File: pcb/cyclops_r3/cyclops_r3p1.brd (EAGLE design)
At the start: 69.8 x 53.3 mm, 48 parts, among them Q1 SUM11006, Q2 IRF510, U1 MCP4921, U2 317-N, U3 ADR03, U4 OP1177, U5 LM324N, U6 ZXTD45

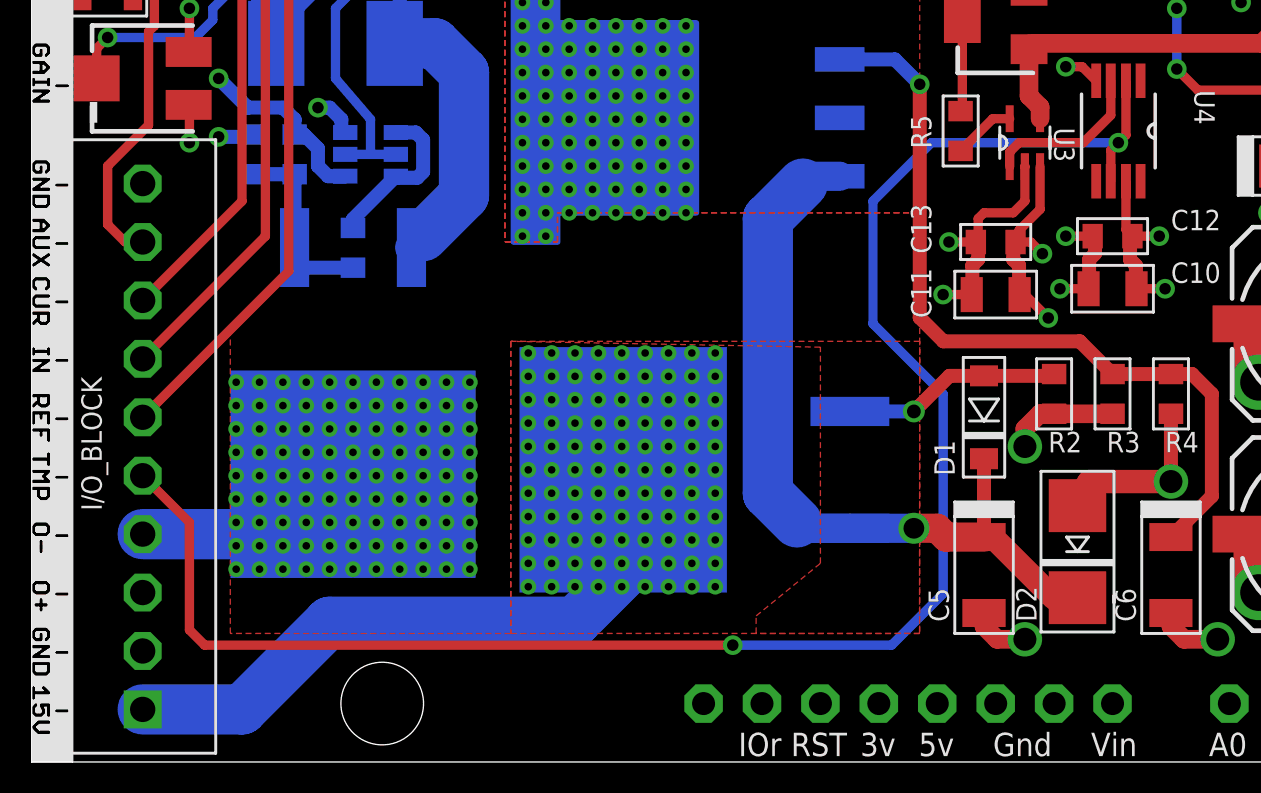
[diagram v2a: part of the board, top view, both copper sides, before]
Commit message: Small routing improvement.
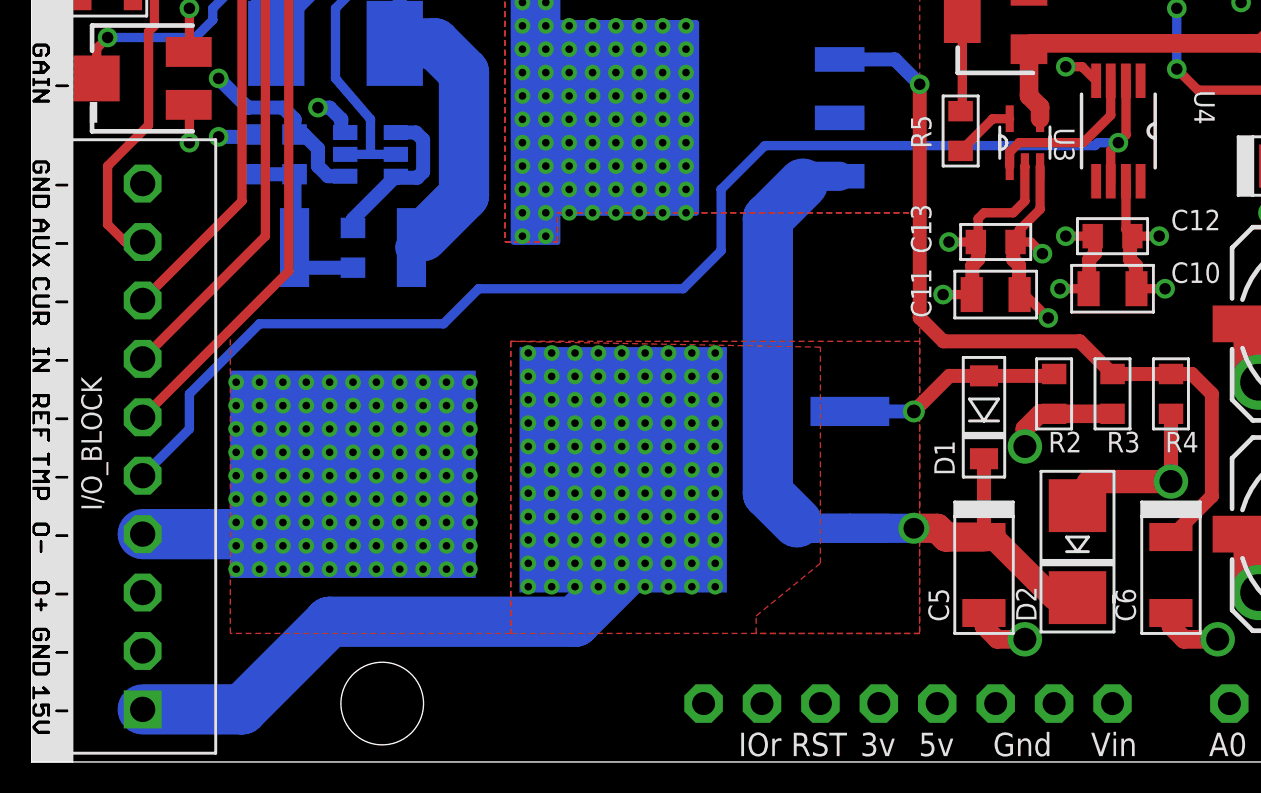
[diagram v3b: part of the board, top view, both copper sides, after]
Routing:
- net VTEMP: track 76.2 -> 55.5 mm, vias 2 -> 1
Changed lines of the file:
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@@
 <layers>
 <layer number="1" name="Top" color="4" fill="1" visible="yes" active="yes"/>
-<layer number="2" name="Route2" color="1" fill="3" visible="yes" active="yes"/>
+<layer number="2" name="Route2" color="1" fill="3" visible="no" active="yes"/>
 <layer number="3" name="Route3" color="4" fill="3" visible="no" active="no"/>
 <layer number="4" name="Route4" color="1" fill="4" visible="no" active="no"/>
@@
 <layer number="13" name="Route13" color="4" fill="5" visible="no" active="no"/>
 <layer number="14" name="Route14" color="1" fill="6" visible="no" active="no"/>
-<layer number="15" name="Route15" color="4" fill="6" visible="yes" active="yes"/>
-<layer number="16" name="Bottom" color="1" fill="1" visible="yes" active="yes"/>
-<layer number="17" name="Pads" color="2" fill="1" visible="yes" active="yes"/>
-<layer number="18" name="Vias" color="2" fill="1" visible="yes" active="yes"/>
-<layer number="19" name="Unrouted" color="6" fill="1" visible="yes" active="yes"/>
-<layer number="20" name="Dimension" color="15" fill="1" visible="yes" active="yes"/>
-<layer number="21" name="tPlace" color="7" fill="1" visible="yes" active="yes"/>
-<layer number="22" name="bPlace" color="7" fill="1" visible="yes" active="yes"/>
-<layer number="23" name="tOrigins" color="15" fill="1" visible="yes" active="yes"/>
-<layer number="24" name="bOrigins" color="15" fill="1" visible="yes" active="yes"/>
-<layer number="25" name="tNames" color="7" fill="1" visible="yes" active="yes"/>
-<layer number="26" name="bNames" color="7" fill="1" visible="yes" active="yes"/>
-<layer number="27" name="tValues" color="7" fill="1" visible="yes" active="yes"/>
-<layer number="28" name="bValues" color="7" fill="1" visible="yes" active="yes"/>
+<layer number="15" name="Route15" color="4" fill="6" visible="no" active="yes"/>
+<layer number="16" name="Bottom" color="1" fill="1" visible="no" active="yes"/>
+<layer number="17" name="Pads" color="2" fill="1" visible="no" active="yes"/>
+<layer number="18" name="Vias" color="2" fill="1" visible="no" active="yes"/>
+<layer number="19" name="Unrouted" color="6" fill="1" visible="no" active="yes"/>
+<layer number="20" name="Dimension" color="15" fill="1" visible="no" active="yes"/>
+<layer number="21" name="tPlace" color="7" fill="1" visible="no" active="yes"/>
+<layer number="22" name="bPlace" color="7" fill="1" visible="no" active="yes"/>
+<layer number="23" name="tOrigins" color="15" fill="1" visible="no" active="yes"/>
+<layer number="24" name="bOrigins" color="15" fill="1" visible="no" active="yes"/>
+<layer number="25" name="tNames" color="7" fill="1" visible="no" active="yes"/>
+<layer number="26" name="bNames" color="7" fill="1" visible="no" active="yes"/>
+<layer number="27" name="tValues" color="7" fill="1" visible="no" active="yes"/>
+<layer number="28" name="bValues" color="7" fill="1" visible="no" active="yes"/>
 <layer number="29" name="tStop" color="7" fill="3" visible="yes" active="yes"/>
 <layer number="30" name="bStop" color="7" fill="6" visible="no" active="yes"/>
@@
 <wire x1="45.6438" y1="26.5938" x2="45.6438" y2="25.2476" width="0.4064" layer="1"/>
 <via x="45.974" y="26.924" extent="1-16" drill="0.5"/>
-<wire x1="45.974" y1="26.924" x2="37.846" y2="26.924" width="0.4064" layer="16"/>
+<wire x1="45.974" y1="26.924" x2="45.085" y2="26.924" width="0.4064" layer="16"/>
+<wire x1="45.085" y1="26.924" x2="44.958" y2="26.797" width="0.4064" layer="16"/>
+<wire x1="44.958" y1="26.797" x2="30.607" y2="26.797" width="0.4064" layer="16"/>
 <contactref element="I/O_BLOCK" pad="P$5"/>
-<wire x1="37.846" y1="26.924" x2="35.306" y2="24.384" width="0.4064" layer="16"/>
-<wire x1="35.306" y1="24.384" x2="35.306" y2="19.05" width="0.4064" layer="16"/>
-<wire x1="35.306" y1="19.05" x2="38.354" y2="16.002" width="0.4064" layer="16"/>
-<wire x1="38.354" y1="16.002" x2="38.354" y2="7.317803125" width="0.4064" layer="16"/>
-<wire x1="38.354" y1="7.317803125" x2="36.116196875" y2="5.08" width="0.4064" layer="16"/>
-<wire x1="36.116196875" y1="5.08" x2="29.21" y2="5.08" width="0.4064" layer="16"/>
-<wire x1="29.21" y1="5.08" x2="6.249809375" y2="5.08" width="0.4064" layer="1"/>
-<wire x1="6.249809375" y1="5.08" x2="5.588" y2="5.741809375" width="0.4064" layer="1"/>
-<wire x1="5.588" y1="5.741809375" x2="5.588" y2="10.414" width="0.4064" layer="1"/>
-<wire x1="5.588" y1="10.414" x2="3.556" y2="12.446" width="0.4064" layer="1"/>
 <wire x1="45.6438" y1="26.5938" x2="45.974" y2="26.924" width="0.4064" layer="1"/>
 <wire x1="45.974" y1="26.924" x2="46.3042" y2="27.2542" width="0.4064" layer="1"/>
-<via x="29.21" y="5.08" extent="1-16" drill="0.5"/>
+<wire x1="30.607" y1="26.797" x2="28.702" y2="24.892" width="0.4064" layer="16"/>
+<wire x1="28.702" y1="24.892" x2="28.702" y2="22.225" width="0.4064" layer="16"/>
+<wire x1="28.702" y1="22.225" x2="27.051" y2="20.574" width="0.4064" layer="16"/>
+<wire x1="27.051" y1="20.574" x2="18.161" y2="20.574" width="0.4064" layer="16"/>
+<wire x1="18.161" y1="20.574" x2="16.637" y2="19.05" width="0.4064" layer="16"/>
+<wire x1="16.637" y1="19.05" x2="8.636" y2="19.05" width="0.4064" layer="16"/>
+<wire x1="8.636" y1="19.05" x2="5.588" y2="16.002" width="0.4064" layer="16"/>
+<wire x1="5.588" y1="16.002" x2="5.588" y2="14.478" width="0.4064" layer="16"/>
+<wire x1="5.588" y1="14.478" x2="3.556" y2="12.446" width="0.4064" layer="16"/>
 </signal>
 <signal name="VCTL">

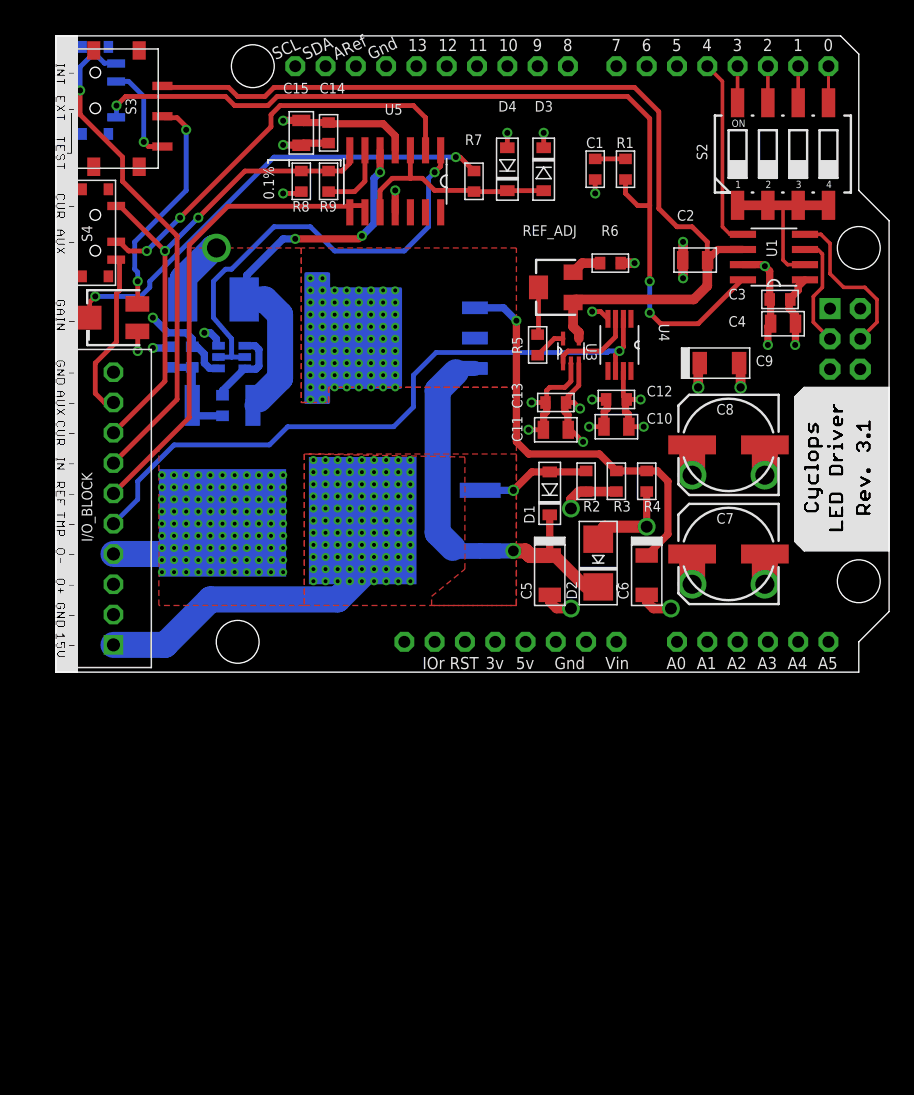
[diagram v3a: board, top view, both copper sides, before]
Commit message: Added a low profile BNC connection for getting input from an amplified photodiode.
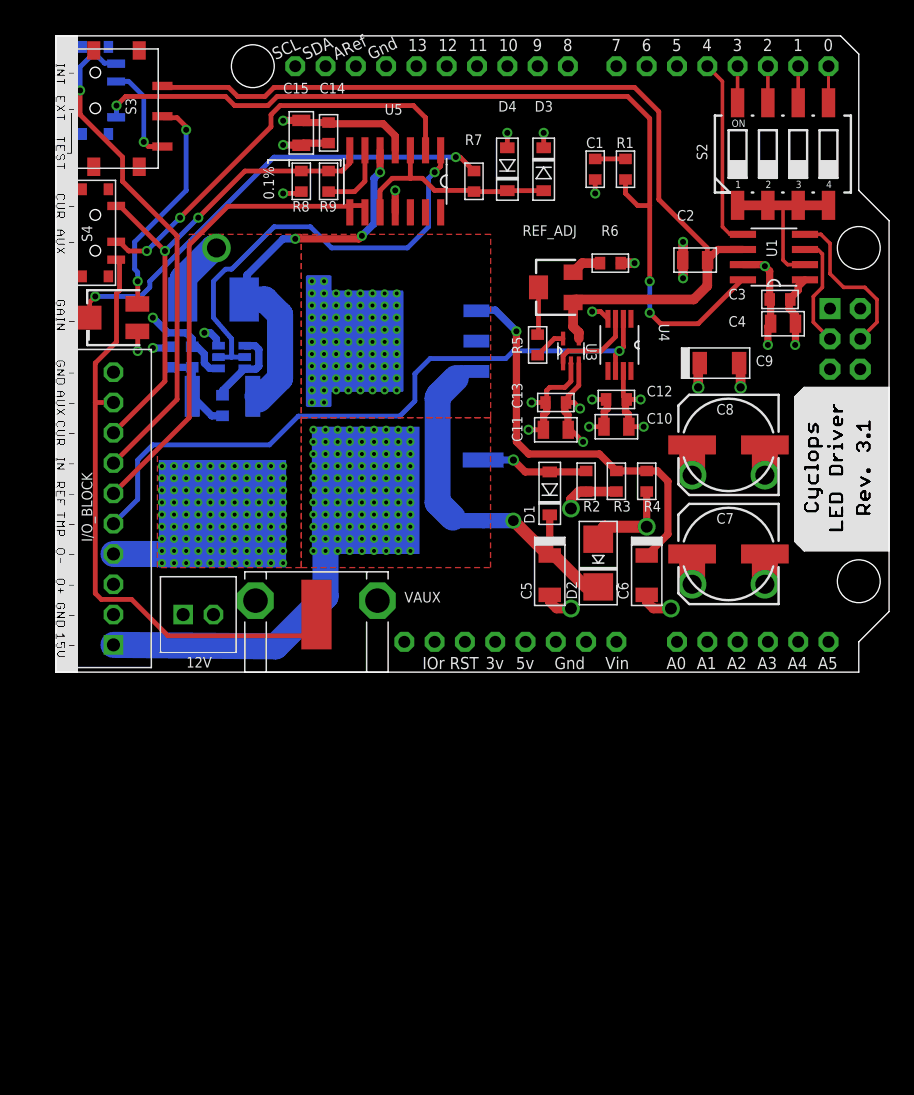
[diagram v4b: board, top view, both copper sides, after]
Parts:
- added 12V: SCREW2, cyclops:SCREW2
- added VAUX: (no value), cyclops:361V509E
- moved Q1 2.55 mm to (29.2, 15.2)
- moved Q2 0.76 mm to (12.7, 17.8)
- moved U2 0.28 mm to (26.8, 27.7)
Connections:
- net +12V: now also 12V.P$2
- net GND: now also 12V.P$1, VAUX.2, VAUX.3
- net VAUX: now also VAUX.1
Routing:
- net VAUX: track 14.0 -> 54.9 mm
- net LED-: track 10.4 -> 18.7 mm
- net +15V: track 28.8 -> 32.0 mm
- net +15V_RECT: track 34.9 -> 33.0 mm
- net N$13: track 8.60 -> 7.42 mm
- net VTEMP: track 55.5 -> 56.3 mm
- net REFA: track 79.1 -> 78.4 mm
- net N$72: track 35.1 -> 34.4 mm

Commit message: Added a note concerning the location of the MOSFET pre-biasing.
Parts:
- R3: value 1.8k -> 2.1k
- R4: value 240k -> 240
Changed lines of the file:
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@@
 <attribute name="VALUE" x="42.418" y="8.128" size="0.889" layer="27" font="vector" ratio="18" rot="R90"/>
 </element>
-<element name="R3" library="cyclops" package="0603" value="1.8k" x="45.72" y="16.002" smashed="yes" rot="R90">
+<element name="R3" library="cyclops" package="0603" value="2.1k" x="45.72" y="16.002" smashed="yes" rot="R90">
 <attribute name="MN" value="Panasonic" x="45.72" y="16.002" size="1.778" layer="27" rot="R90" display="off"/>
 <attribute name="DK" value="PxxxxHTR-ND" x="45.72" y="16.002" size="1.778" layer="27" rot="R90" display="off"/>
@@
 <attribute name="VALUE" x="44.196" y="17.78" size="0.889" layer="27" font="vector" ratio="18"/>
 </element>
-<element name="R4" library="cyclops" package="0603" value="240k" x="48.26" y="16.002" smashed="yes" rot="R270">
+<element name="R4" library="cyclops" package="0603" value="240" x="48.26" y="16.002" smashed="yes" rot="R270">
 <attribute name="MN" value="Panasonic" x="48.26" y="16.002" size="1.778" layer="27" rot="R270" display="off"/>
 <attribute name="DK" value="PxxxxHTR-ND" x="48.26" y="16.002" size="1.778" layer="27" rot="R270" display="off"/>

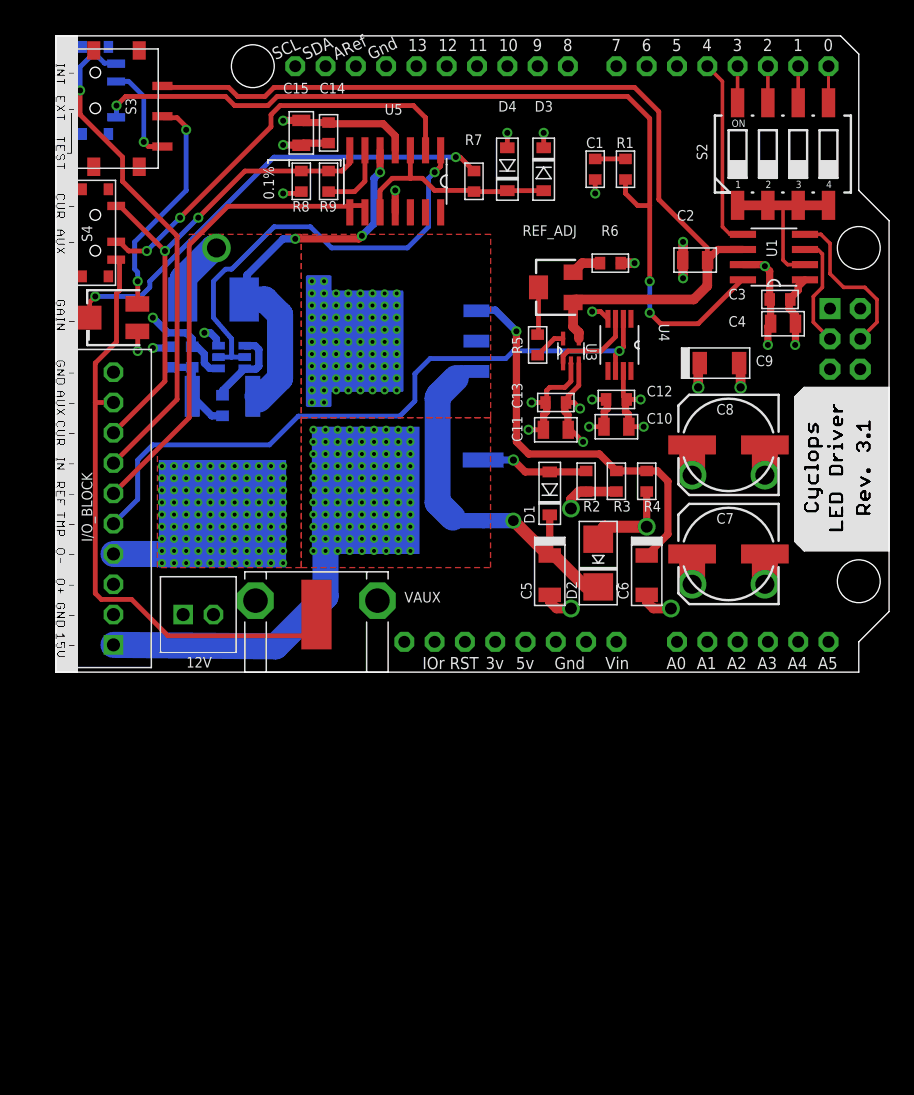
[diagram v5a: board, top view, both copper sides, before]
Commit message: Put the circuit on the breadboard today and found several mistakes/improvments to the design. I implemented some of those here and documented what else needs to be done in the notes.
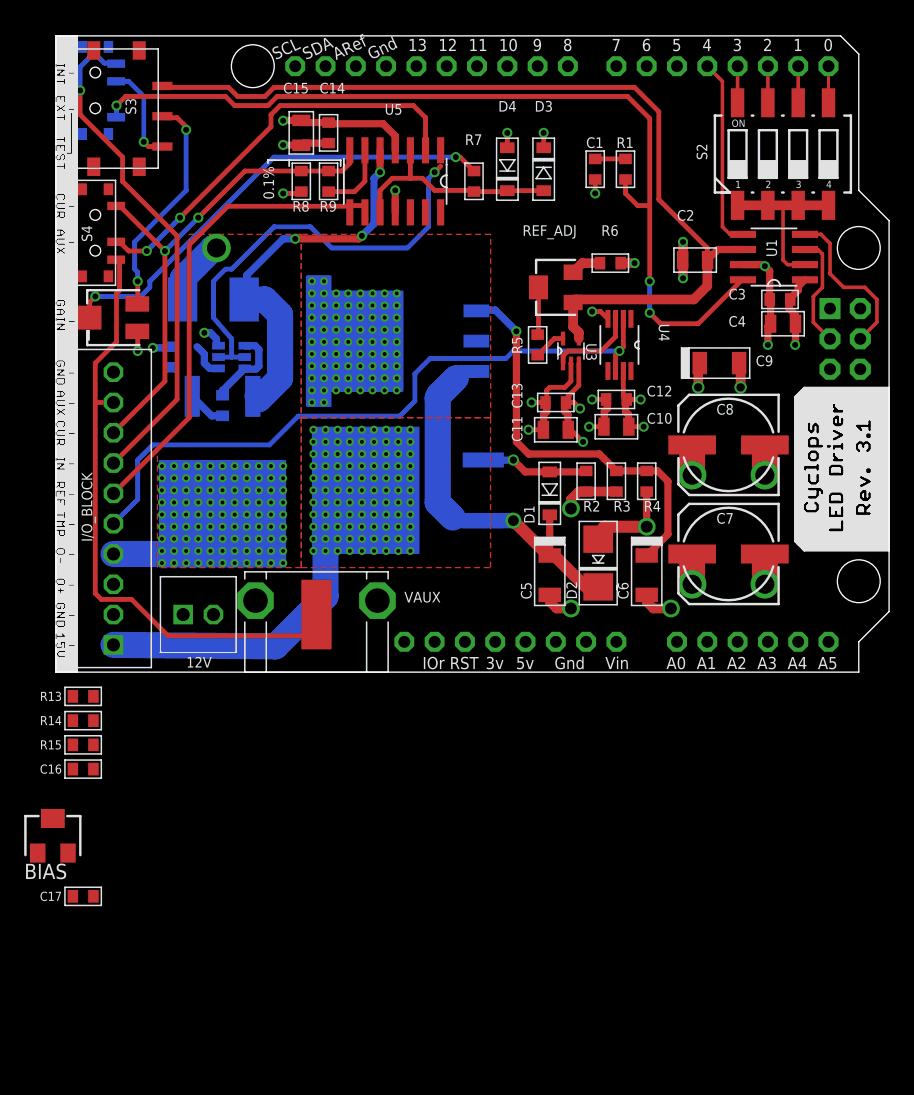
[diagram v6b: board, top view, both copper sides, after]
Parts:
- removed R11: 1.1k, cyclops:0603
- added BIAS: 10k, cyclops:SM-42/43W
- added C16, C17: .1uF, cyclops:0603
- added R13, R14, R15: 1k, cyclops:0603
- R10: value 560 -> 10
- R12: value 560 -> 1k
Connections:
- net _VCTL renamed VCTL_PRE
- removed net N$3: U5.1, U6.2, U6.5
- new net AGND: BIAS.3, C17.2
- new net N$4: BIAS.2, U5.1, U6.2, U6.5
- new net N$8: R14.2, U5.13
- new net REFA2X: C16.1, R15.2, S3.1
- new net VREFA2X: R13.1, R14.1, R15.1, U5.14
- net +12V: now also BIAS.1, C17.1; no longer R11.2
- net GND: now also C16.2, R13.2
- net N$13: no longer R11.1
- net REFA: now also U5.12; no longer S3.1
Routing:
- net N$3: track 37.5 -> 0.00 mm, vias 1 -> 0
- net N$4: track 0.00 -> 36.2 mm, vias 0 -> 1
- net +12V: track 52.8 -> 47.7 mm, vias 87 -> 86
- net N$13: track 7.42 -> 3.22 mm
